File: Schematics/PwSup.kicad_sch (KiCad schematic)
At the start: 21 parts, among them J3 Phase, J4 PX Ph, J5 PXB10C, J6 Neutral, J7 Px N, SW2 SW_SPST

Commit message: footprints assigned
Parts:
- CE2, CE3: footprint (none) -> Capacitor_THT:CP_Radial_D14.0mm_P7.50mm
- F1: footprint (none) -> Fuse:Fuseholder_Clip-5x20mm_Littelfuse_520_Inline_P20.50x5.80mm_D1.30mm_Horizontal
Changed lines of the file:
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@@
 			)
 		)
-		(property "Footprint" ""
+		(property "Footprint" "Capacitor_THT:CP_Radial_D14.0mm_P7.50mm"
 			(at 72.39 56.8452 0)
 			(hide yes)
@@
 			)
 		)
-		(property "Footprint" ""
+		(property "Footprint" "Capacitor_THT:CP_Radial_D14.0mm_P7.50mm"
 			(at 95.25 56.8452 0)
 			(hide yes)
@@
 			)
 		)
-		(property "Footprint" ""
+		(property "Footprint" "Fuse:Fuseholder_Clip-5x20mm_Littelfuse_520_Inline_P20.50x5.80mm_D1.30mm_Horizontal"
 			(at 35.56 62.738 90)
 			(hide yes)

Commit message: directory cleared, Schem upd
The input mixer changed from passive to active(TL072)
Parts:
- added U3: TL072, symbol Amplifier_Operational:TL072
- renumbered D1 to D7
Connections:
- net VCC: now also U3.8 (V+)
- net VEE: now also U3.4 (V-)
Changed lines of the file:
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@@
+	(wire
+		(pts
+			(xy 49.53 114.3) (xy 43.18 114.3)
+		)
+		(stroke
+			(width 0)
+			(type default)
+		)
+	)
 	(wire
 		(pts
@@
 		(pts
 			(xy 72.39 80.01) (xy 74.93 80.01)
+		)
+		(stroke
+			(width 0)
+			(type default)
+		)
+	)
+	(wire
+		(pts
+			(xy 24.13 114.3) (xy 27.94 114.3)
 		)
 		(stroke
@@
 	)
 	(label "VCC"
+		(at 24.13 114.3 0)
+		(effects
+			(font
+				(size 1.27 1.27)
+			)
+			(justify left bottom)
+		)
+	)
+	(label "VCC"
 		(at 24.13 91.44 0)
 		(effects
@@
 			)
 			(justify left bottom)
+		)
+	)
+	(label "VEE"
+		(at 49.53 114.3 180)
+		(effects
+			(font
+				(size 1.27 1.27)
+			)
+			(justify right bottom)
 		)
 	)
@@
 	)
 	(symbol
+		(lib_id "Amplifier_Operational:TL072")
+		(at 35.56 111.76 90)
+		(unit 3)
+		(body_style 1)
+		(exclude_from_sim no)
+		(in_bom yes)
+		(on_board yes)
+		(in_pos_files yes)
+		(dnp no)
+		(fields_autoplaced yes)
+		(property "Reference" "U3"
+			(at 35.56 109.22 90)
+			(show_name no)
+			(do_not_autoplace no)
+			(effects
+				(font
+					(size 1.27 1.27)
+				)
+			)
+		)
+		(property "Value" "TL072"
+			(at 35.56 111.76 90)
+			(show_name no)
+			(do_not_autoplace no)
+			(effects
+				(font
+					(size 1.27 1.27)
+				)
+			)
+		)
+		(property "Footprint" ""
+			(at 35.56 111.76 0)
+			(hide yes)
+			(show_name no)
+			(do_not_autoplace no)
+			(effects
+				(font
+					(size 1.27 1.27)
+				)
+			)
+		)
+		(property "Datasheet" "http://www.ti.com/lit/ds/symlink/tl071.pdf"
+			(at 35.56 111.76 0)
+			(hide yes)
+			(show_name no)
+			(do_not_autoplace no)
+			(effects
+				(font
+					(size 1.27 1.27)
+				)
+			)
+		)
+		(property "Description" "Dual Low-Noise JFET-Input Operational Amplifiers, DIP-8/SOIC-8"
+			(at 35.56 111.76 0)
+			(hide yes)
+			(show_name no)
+			(do_not_autoplace no)
+			(effects
+				(font
+					(size 1.27 1.27)
+				)
+			)
+		)
+		(pin "6"
+		)
+		(pin "4"
+		)
+		(pin "3"
+		)
+		(pin "2"
+		)
+		(pin "1"
+		)
+		(pin "7"
+		)
+		(pin "8"
+		)
+		(pin "5"
+		)
+		(instances
+			(project "AMP-MA"
+				(path "/4094031b-a9da-4ac5-aaa1-42b342c92a3e/50fcec93-e12d-4852-998b-ff512e6cbf1d"
+					(reference "U3")
+					(unit 3)
+				)
+			)
+		)
+	)
+	(symbol
 		(lib_id "Device:C_Polarized")
 		(at 76.2 55.88 270)
@@
 		(in_pos_files yes)
 		(dnp no)
-		(property "Reference" "D1"
+		(property "Reference" "D7"
 			(at 92.964 48.514 0)
 			(show_name no)
@@
 			(project "AMP-MA"
 				(path "/4094031b-a9da-4ac5-aaa1-42b342c92a3e/50fcec93-e12d-4852-998b-ff512e6cbf1d"
-					(reference "D1")
+					(reference "D7")
 					(unit 1)
 				)

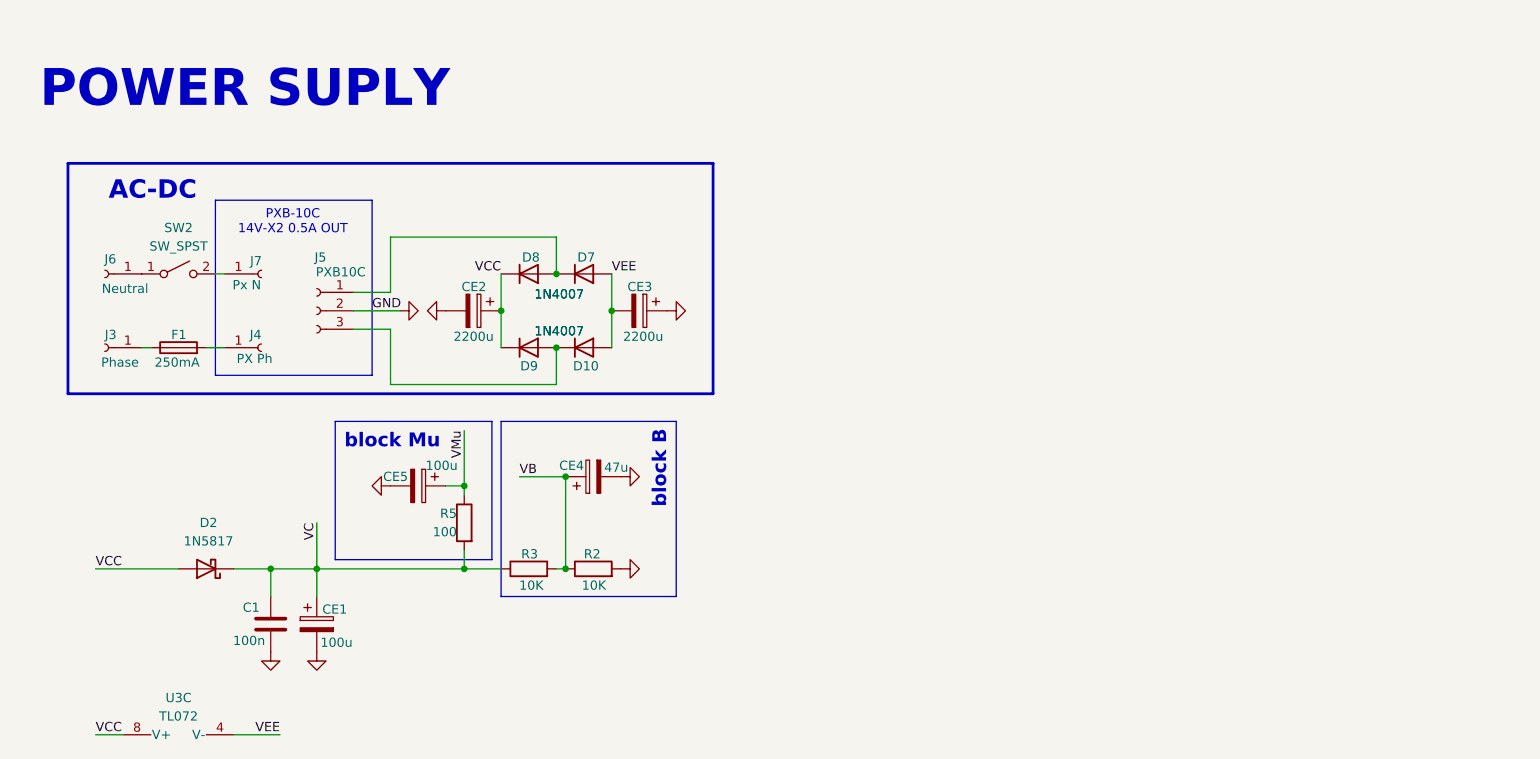
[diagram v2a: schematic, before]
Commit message: Schem upd
The LED is powered by the low voltage supply, not by the effect
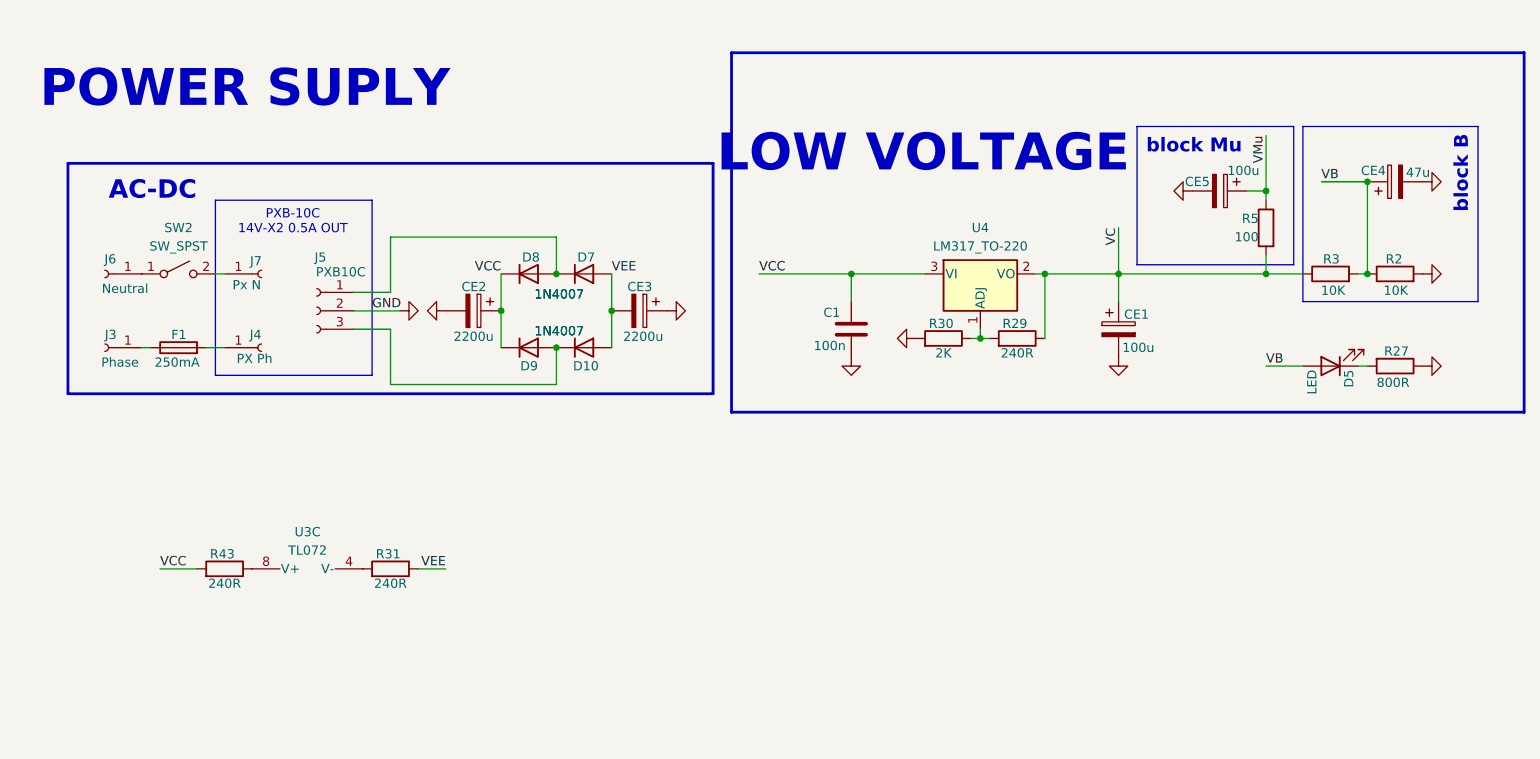
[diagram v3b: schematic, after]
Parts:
- removed D2: 1N5817, Diode_THT:D_DO-41_SOD81_P10.16mm_Horizontal, symbol Diode:1N5817
- added D5: LED, LED_THT:LED_BL-FL7680RGB, symbol Device:LED
- added R27: 800R, Resistor_THT:R_Axial_DIN0207_L6.3mm_D2.5mm_P10.16mm_Horizontal, symbol Device:R
- added R29, R31, R43: 240R, Resistor_THT:R_Axial_DIN0207_L6.3mm_D2.5mm_P10.16mm_Horizontal, symbol Device:R
- added R30: 2K, Resistor_THT:R_Axial_DIN0207_L6.3mm_D2.5mm_P10.16mm_Horizontal, symbol Device:R
- added U4: LM317_TO-220, Package_TO_SOT_THT:TO-220-3_Horizontal_TabDown, symbol Regulator_Linear:LM317_TO-220
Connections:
- net GND: now also R27.1, R30.2
- net VB: now also D5.2 (A)
- net VC: now also R29.1, U4.2 (VO); no longer C1.1
- net VCC: now also C1.1, R43.2, U4.3 (VI); no longer U3.8 (V+)
- net VEE: now also R31.1; no longer U3.4 (V-)
- new net: R31.2, U3.4 (V-)
- new net: D5.1 (K), R27.2
- new net: R29.2, R30.1, U4.1 (ADJ)
- new net: R43.1, U3.8 (V+)
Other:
- note added: "LOW VOLTAGE"
- moved on the sheet: CE1, CE4, CE5, R2, R3, R5, U3C

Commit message: Schem upd
Managed power supply for TL072
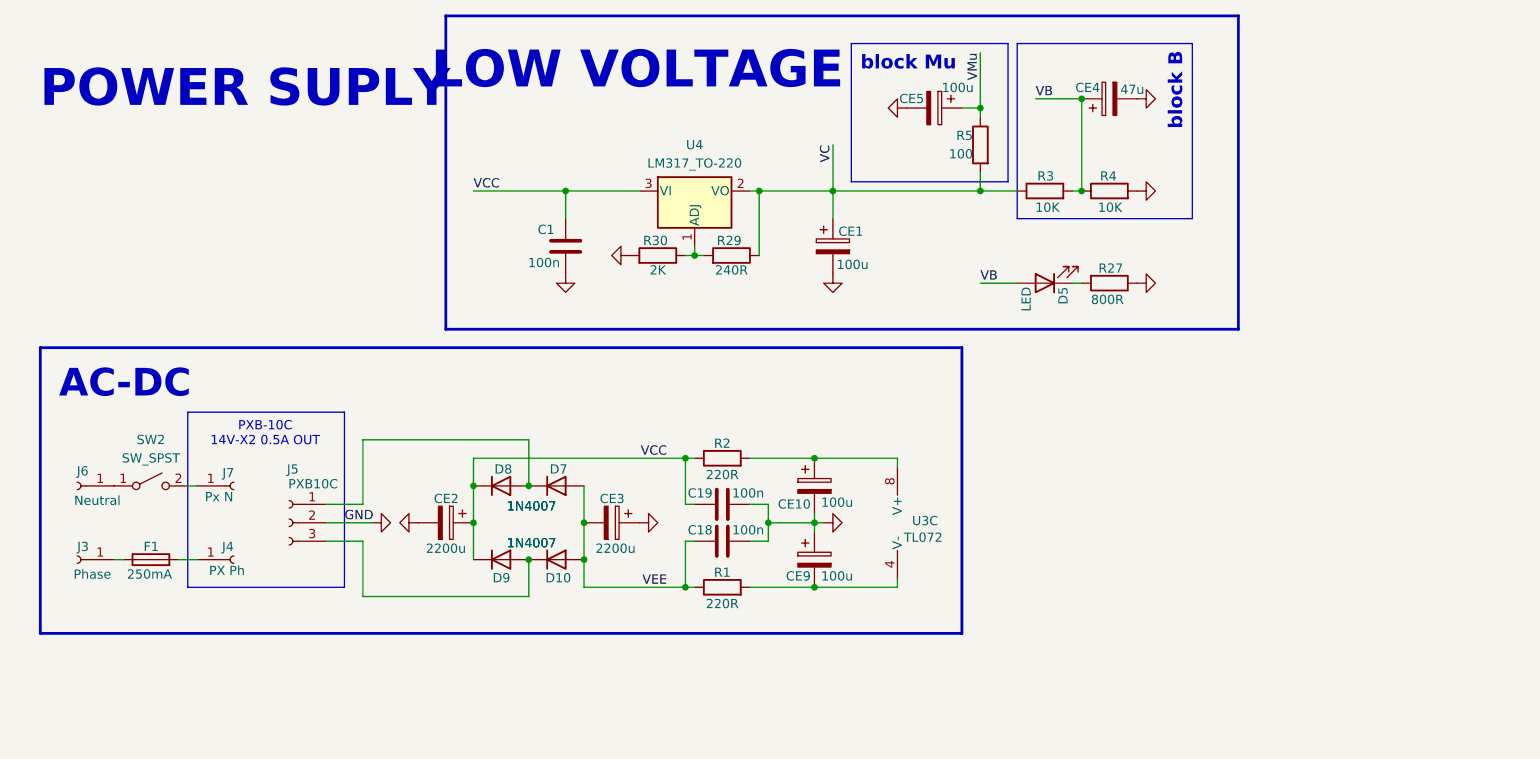
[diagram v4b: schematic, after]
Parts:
- removed R31, R43: 240R, Resistor_THT:R_Axial_DIN0207_L6.3mm_D2.5mm_P10.16mm_Horizontal, symbol Device:R
- added C18, C19: 100n, symbol Device:C
- added CE10, CE9: 100u, Capacitor_THT:CP_Radial_D14.0mm_P7.50mm, symbol Device:C_Polarized
- added R1: 220R, symbol Device:R
- added R4: 10K, Resistor_THT:R_Axial_DIN0207_L6.3mm_D2.5mm_P7.62mm_Horizontal, symbol Device:R
- R2: value 10K -> 220R; footprint Resistor_THT:R_Axial_DIN0207_L6.3mm_D2.5mm_P7.62mm_Horizontal -> (none)
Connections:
- net GND: now also C18.2, C19.2, CE10.2, CE9.1, R4.2; no longer R2.2
- net VB: now also R4.1; no longer R2.1
- net VCC: now also R2.1, C19.1
- net VEE: now also C18.1, R1.1
- net at U3.4 (V-): now also CE9.2, R1.2
- net at U3.8 (V+): now also R2.2, CE10.1
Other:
- moved on the sheet: CE2, CE3, D10, D7, D8, D9, F1, J3, J4, J5, J6, J7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

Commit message: Schem upd & added .gitignore
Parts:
- removed CE10, CE9: 100u, Capacitor_THT:CP_Radial_D14.0mm_P7.50mm, symbol Device:C_Polarized
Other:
- moved on the sheet: U3C

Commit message: Lib & Schematic upd
Jack connector symbol update. Made basic layout has been made
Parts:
- C18, C19: footprint (none) -> Capacitor_THT:C_Disc_D7.0mm_W2.5mm_P5.00mm
- D5: footprint LED_THT:LED_BL-FL7680RGB -> LED_THT:LED_D3.0mm_Horizontal_O6.35mm_Z6.0mm
- J5: footprint Jumper:SolderJumper-2_P1.3mm_Open_TrianglePad1.0x1.5mm -> Connector_JST:JST_PH_B3B-PH-K_1x03_P2.00mm_Vertical
- U3: footprint (none) -> Package_DIP:DIP-8_W7.62mm
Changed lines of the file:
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@@
 			)
 		)
-		(property "Footprint" ""
+		(property "Footprint" "Package_DIP:DIP-8_W7.62mm"
 			(at 125.73 85.09 0)
 			(hide yes)
@@
 			)
 		)
-		(property "Footprint" "Jumper:SolderJumper-2_P1.3mm_Open_TrianglePad1.0x1.5mm"
+		(property "Footprint" "Connector_JST:JST_PH_B3B-PH-K_1x03_P2.00mm_Vertical"
 			(at 50.8 85.09 0)
 			(hide yes)
@@
 			)
 		)
-		(property "Footprint" "LED_THT:LED_BL-FL7680RGB"
+		(property "Footprint" "LED_THT:LED_D3.0mm_Horizontal_O6.35mm_Z6.0mm"
 			(at 154.94 52.07 0)
 			(hide yes)
@@
 			)
 		)
-		(property "Footprint" ""
+		(property "Footprint" "Capacitor_THT:C_Disc_D7.0mm_W2.5mm_P5.00mm"
 			(at 114.3 86.6648 0)
 			(hide yes)
@@
 			)
 		)
-		(property "Footprint" ""
+		(property "Footprint" "Capacitor_THT:C_Disc_D7.0mm_W2.5mm_P5.00mm"
 			(at 114.3 81.5848 0)
 			(hide yes)
